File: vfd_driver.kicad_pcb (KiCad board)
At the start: 2 copper layers, 89.5 x 45.3 mm, 34 parts, among them J1 Input, J2 futaba_7_lt_44z, J3 High Volt, J4 FIL_n, J5 FIL_p, Q3 BC817, Q4 BC807, Q5 BC817, Q6 BC807, U1 74HC595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

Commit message: before adding lt1073
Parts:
- removed C1: 10u, Capacitor_THT:CP_Radial_D8.0mm_P3.80mm
- removed C2: 100n, Capacitor_SMD:C_0805_2012Metric_Pad1.15x1.40mm_HandSolder
- removed J4: FIL_n, Connector_Pin:Pin_D1.4mm_L8.5mm_W2.8mm_FlatFork
- removed J5: FIL_p, Connector_Pin:Pin_D1.4mm_L8.5mm_W2.8mm_FlatFork
- removed L2: 33, Inductor_SMD:L_1206_3216Metric_Pad1.42x1.75mm_HandSolder
- removed Q3, Q5: BC817, Package_TO_SOT_SMD:SOT-23
- removed Q4, Q6: BC807, Package_TO_SOT_SMD:SOT-23
- removed R10, R7, R8: 33k, Resistor_SMD:R_0805_2012Metric_Pad1.15x1.40mm_HandSolder
- removed R12, R13: 0, Resistor_SMD:R_1206_3216Metric
- removed R6, R9: 100k, Resistor_SMD:R_0805_2012Metric_Pad1.15x1.40mm_HandSolder
- removed U2, U3, U4: 74HC595, Package_SO:SOIC-16_3.9x9.9mm_P1.27mm
- removed U5, U6, U7: TBD62783A, Package_SO:SOP-18_7.0x12.5mm_P1.27mm
- added C4: 10u/63v, Capacitor_THT:CP_Radial_D8.0mm_P5.00mm, F.Cu at (41.9, 56.6)
- added C6: 4n7, Capacitor_SMD:C_0805_2012Metric_Pad1.15x1.40mm_HandSolder, B.Cu at (63.1, 46.6)
- added C7: 1u, Capacitor_THT:C_Rect_L7.0mm_W2.0mm_P5.00mm, F.Cu at (57.9, 44.2)
- added C8: 100n, Capacitor_THT:C_Rect_L7.0mm_W2.0mm_P5.00mm, F.Cu at (53.0, 41.4)
- added C9: 10n, Capacitor_SMD:C_0805_2012Metric_Pad1.15x1.40mm_HandSolder, B.Cu at (45.1, 43.0)
- added D2: SS14, Diode_SMD:D_SMA_Handsoldering, B.Cu at (51.1, 50.7)
- added D3: 1N4148, Diode_SMD:D_MiniMELF, B.Cu at (55.6, 37.9)
- added L1: 330, Choke_SMD:Choke_CD75, B.Cu at (42.8, 50.0)
- added Q1: IRLZ34, Package_TO_SOT_THT:TO-220-3_Vertical, F.Cu at (33.5, 51.2)
- added R14: 0, Resistor_SMD:R_1206_3216Metric, B.Cu at (44.5, 36.4)
- added R15: 22k, Resistor_SMD:R_0805_2012Metric_Pad1.15x1.40mm_HandSolder, B.Cu at (63.1, 43.9)
- added R16: 18, Resistor_SMD:R_1206_3216Metric_Pad1.42x1.75mm_HandSolder, B.Cu at (64.8, 53.2)
- added R17: 18, Resistor_SMD:R_1206_3216Metric_Pad1.42x1.75mm_HandSolder, B.Cu at (55.8, 59.3)
- added R18: 4k7, Resistor_SMD:R_0805_2012Metric_Pad1.15x1.40mm_HandSolder, B.Cu at (52.6, 37.5)
- added R3: 22k, Resistor_SMD:R_0805_2012Metric_Pad1.15x1.40mm_HandSolder, B.Cu at (64.1, 41.4)
- added R4: 10k, Resistor_SMD:R_0805_2012Metric_Pad1.15x1.40mm_HandSolder, B.Cu at (58.2, 47.4)
- added U8: LM555, Package_DIP:DIP-8_W7.62mm_Socket_LongPads, F.Cu at (40.8, 33.5)
- C5: value 10n -> 100n
- D1: value SD103BW -> SD_103BW
- J1: footprint Connector_PinSocket_2.54mm:PinSocket_1x07_P2.54mm_Vertical -> Connector_PinHeader_2.54mm:PinHeader_1x02_P2.54mm_Vertical
- J2: value futaba_7_lt_44z -> FIL; footprint Connector_PinSocket_2.54mm:PinSocket_1x34_P2.54mm_Vertical -> Connector_PinHeader_2.54mm:PinHeader_1x02_P2.54mm_Vertical; moved to F.Cu
- J3: value High Volt -> HV
- R1: value 0 -> 1k; footprint Resistor_SMD:R_1206_3216Metric -> Resistor_SMD:R_0805_2012Metric_Pad1.15x1.40mm_HandSolder
- R2: value 0 -> 100k; footprint Resistor_SMD:R_1206_3216Metric -> Resistor_SMD:R_0805_2012Metric_Pad1.15x1.40mm_HandSolder
- R5: value 33k -> 1k
- U1: value 74HC595 -> LM4871; footprint Package_SO:SOIC-16_3.9x9.9mm_P1.27mm -> Package_SO:SOIC-8_3.9x4.9mm_P1.27mm
- moved H2 91.6 mm to (31.6, 58.4)
- moved R2 73.2 mm to (35.3, 41.0)
- moved C5 64.5 mm to (44.7, 31.8), turned to 180 degrees
- moved R5 62.7 mm to (58.5, 37.6), turned to 270 degrees
- moved U1 53.8 mm to (58.2, 53.0), turned to 270 degrees
- moved R1 53.5 mm to (35.3, 38.0)
- moved C3 43.8 mm to (63.8, 34.7), turned to 270 degrees
- moved D1 37.3 mm to (36.7, 47.4), turned to 90 degrees
- moved J2 28.3 mm to (62.5, 59.3)
- moved J3 14.1 mm to (50.0, 59.3), turned to 270 degrees
- moved J1 9.29 mm to (54.7, 32.9), turned to 90 degrees
- moved H1 5.66 mm to (31.6, 33.4)
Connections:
- C3 pad 1: VCC -> +5V
- C5 pad 1: VCC -> +5V
- D1 pad 2: VDD -> GND
- J1 pad 2: VDD -> +5V
- J2 pad 1: Net-(J2-Pad1) -> /FIL_n
- J2 pad 2: (no net) -> /FIL_p
- J3 pad 1: GND -> +36V
- J3 pad 2: +36V -> GND
- R1 pad 1: /SRCLK -> Net-(Q1-Pad1)
- R1 pad 2: /SRCLK -> /HV
- R2 pad 1: /SRCLK -> Net-(Q1-Pad1)
- R2 pad 2: /SRCLK -> GND
- R5 pad 1: /Q4G -> +5V
- U1 pad 1: (no net) -> GND
- U1 pad 2: (no net) -> Net-(C7-Pad1)
- U1 pad 3: (no net) -> Net-(R15-Pad2)
- U1 pad 4: (no net) -> Net-(C6-Pad1)
- U1 pad 5: (no net) -> Net-(R15-Pad1)
- U1 pad 6: /Q4G -> +5V
- U1 pad 7: /Q4H -> GND
- U1 pad 8: GND -> Net-(R17-Pad1)
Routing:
- net VCC: track 119.9 -> 0.00 mm, vias 4 -> 0
- net /~SRCLR: track 109.7 -> 0.00 mm, vias 2 -> 0
- net /RCLK: track 94.4 -> 0.00 mm, vias 6 -> 0
- net /SRCLK: track 93.5 -> 0.00 mm, vias 2 -> 0
- net +5V: track 0.00 -> 81.7 mm
- net +36V: track 95.8 -> 18.2 mm
- net /Q1: track 48.7 -> 0.00 mm, vias 2 -> 0
- net /Q0: track 45.6 -> 0.00 mm, vias 2 -> 0
- net /Q2: track 35.3 -> 0.00 mm, vias 2 -> 0
- net Net-(R15-Pad1): track 0.00 -> 27.1 mm
- net /G1: track 21.3 -> 0.00 mm
- net Net-(C8-Pad1): track 0.00 -> 21.2 mm
- net /S10: track 21.1 -> 0.00 mm
- net /G5: track 19.9 -> 0.00 mm
- net Net-(Q1-Pad1): track 0.00 -> 17.9 mm
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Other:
- board size 89.5 x 45.3 mm -> 41.3 x 32.6 mm
- board text removed: "VFD-DRIVER"

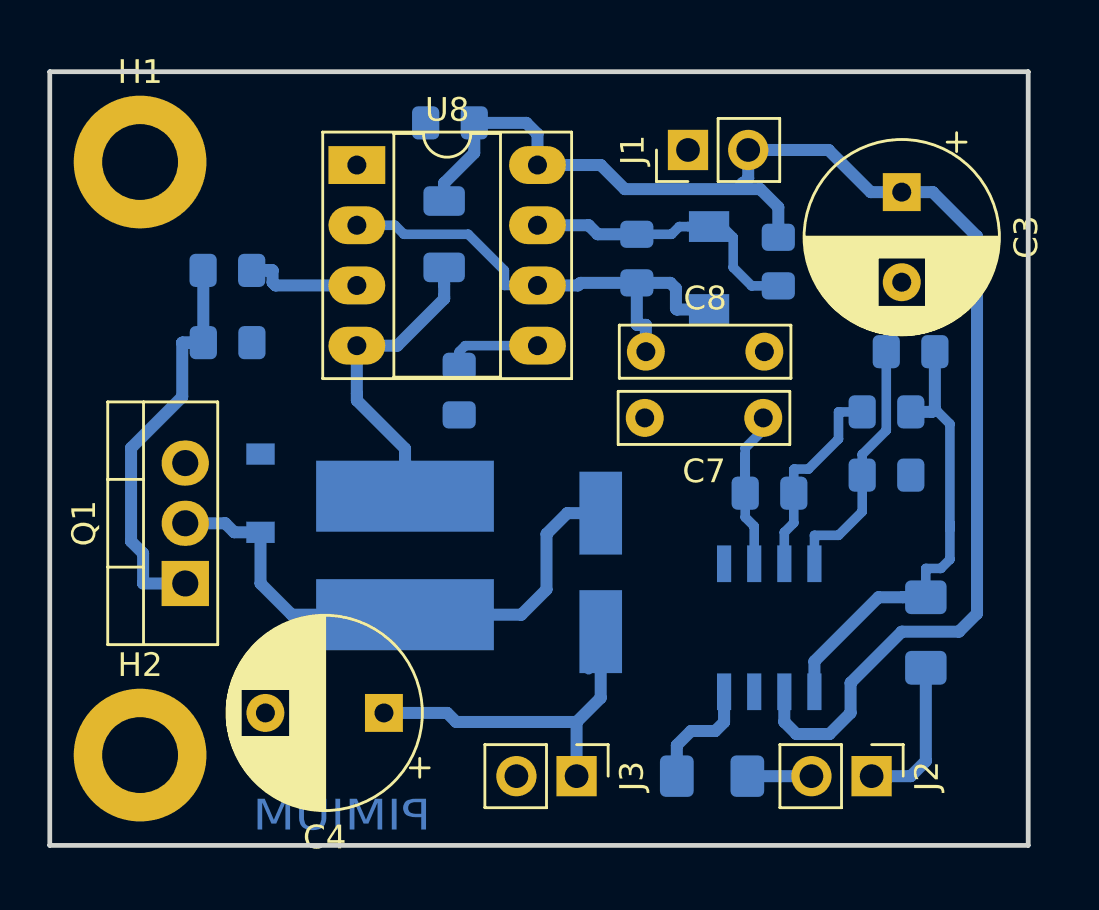
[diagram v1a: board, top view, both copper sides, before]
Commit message: Separated input for the step up driver so ca be supply with 12V.
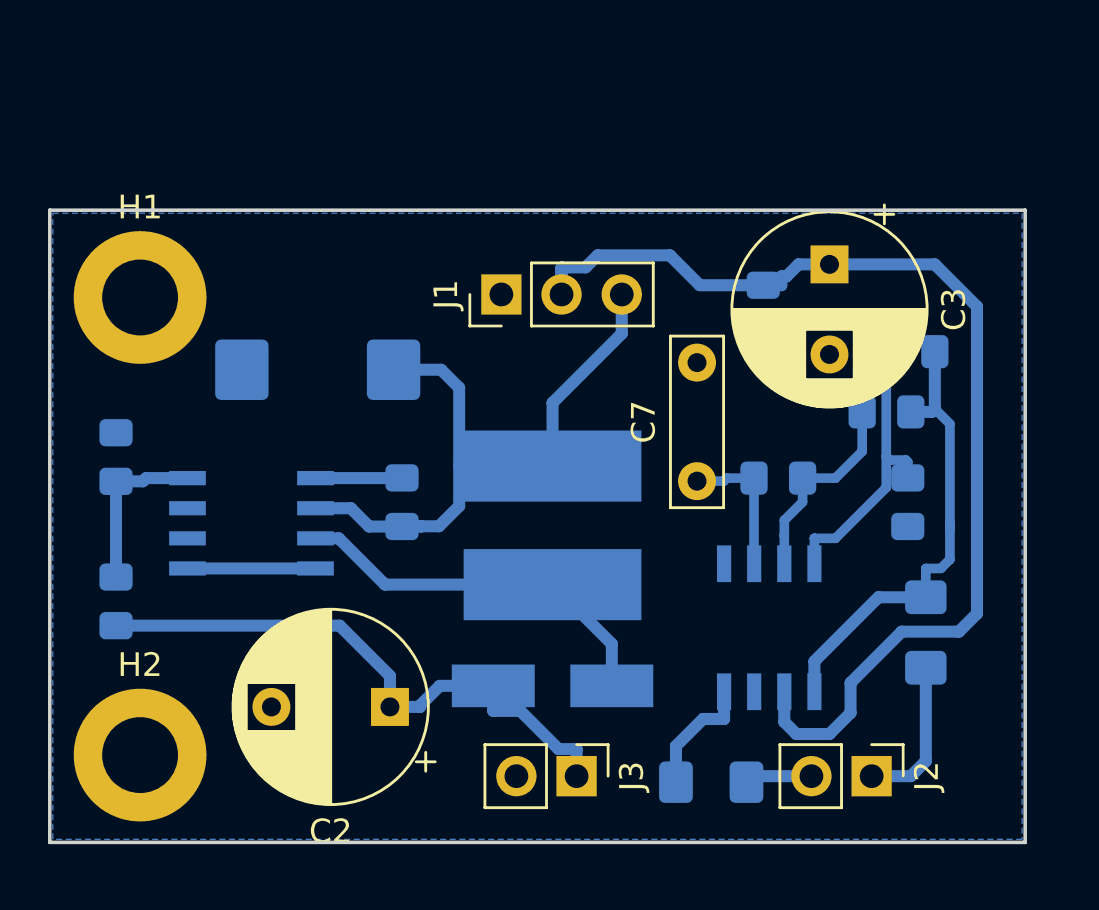
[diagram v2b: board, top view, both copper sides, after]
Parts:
- removed C4: 10u/63v, Capacitor_THT:CP_Radial_D8.0mm_P5.00mm
- removed C8: 100n, Capacitor_THT:C_Rect_L7.0mm_W2.0mm_P5.00mm
- removed C9: 10n, Capacitor_SMD:C_0805_2012Metric_Pad1.15x1.40mm_HandSolder
- removed D2: SS14, Diode_SMD:D_SMA_Handsoldering
- removed D3: 1N4148, Diode_SMD:D_MiniMELF
- removed Q1: IRLZ34, Package_TO_SOT_THT:TO-220-3_Vertical
- removed R14: 0, Resistor_SMD:R_1206_3216Metric
- removed R18: 4k7, Resistor_SMD:R_0805_2012Metric_Pad1.15x1.40mm_HandSolder
- removed U8: LM555, Package_DIP:DIP-8_W7.62mm_Socket_LongPads
- added C1: 100u, Capacitor_Tantalum_SMD:CP_EIA-7343-15_Kemet-W_Pad2.25x2.55mm_HandSolder, B.Cu at (39.1, 42.2)
- added C2: 100u/63v, Capacitor_THT:CP_Radial_D8.0mm_P5.00mm, F.Cu at (42.2, 56.4)
- added U2: LT1073CS, Package_SO:SOIC-8_3.9x4.9mm_P1.27mm, B.Cu at (36.3, 48.6)
- D1: value SD_103BW -> SS14; footprint Diode_SMD:D_SOD-123 -> Diode_SMD:D_SMA_Handsoldering
- J1: value Input -> INPUT; footprint Connector_PinHeader_2.54mm:PinHeader_1x02_P2.54mm_Vertical -> Connector_PinHeader_2.54mm:PinHeader_1x03_P2.54mm_Vertical
- R1: value 1k -> 50
- R2: value 100k -> 1M
- R5: value 1k -> 10k
- moved R5 29.1 mm to (30.6, 45.8)
- moved C5 15.4 mm to (57.9, 39.6), turned to 270 degrees
- moved D1 14.8 mm to (49.0, 55.5), turned to 0 degrees
- moved R1 12.2 mm to (42.7, 47.8), turned to 270 degrees
- moved R2 11.9 mm to (30.6, 51.9), turned to 270 degrees
- moved J1 9.96 mm to (46.9, 39.0)
- moved L1 6.35 mm to (49.0, 48.7)
- moved H1 5.71 mm to (31.6, 39.1)
- moved C3 4.31 mm to (60.7, 37.7)
- moved C7 3.86 mm to (55.1, 46.9), turned to 90 degrees
- moved C6 1.45 mm to (64.0, 47.8), turned to 270 degrees
- moved R4 0.74 mm to (58.5, 46.7)
- moved R17 0.26 mm to (55.7, 59.6)
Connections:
- D1 pad 1: Net-(D1-Pad1) -> +36V
- D1 pad 2: GND -> Net-(D1-Pad2)
- L1 pad 1: +5V -> +12V
- L1 pad 2: Net-(D1-Pad1) -> Net-(D1-Pad2)
- R1 pad 1: Net-(Q1-Pad1) -> Net-(R1-Pad1)
- R1 pad 2: /HV -> +12V
- R2 pad 1: Net-(Q1-Pad1) -> Net-(R2-Pad1)
- R2 pad 2: GND -> +36V
- R5 pad 1: +5V -> GND
- R5 pad 2: Net-(D3-Pad2) -> Net-(R2-Pad1)
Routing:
- net +5V: track 81.7 -> 46.8 mm
- net +12V: track 0.00 -> 27.2 mm
- net Net-(D1-Pad1): track 23.5 -> 0.00 mm
- net Net-(C8-Pad1): track 21.2 -> 0.00 mm
- net Net-(Q1-Pad1): track 17.9 -> 0.00 mm
- net Net-(D1-Pad2): track 0.00 -> 16.1 mm
- net Net-(D3-Pad2): track 13.5 -> 0.00 mm
- net Net-(R2-Pad1): track 0.00 -> 7.11 mm
- net +36V: track 18.2 -> 25.0 mm
- net /HV: track 5.41 -> 0.00 mm
- net GND: track 0.00 -> 5.40 mm
- net Net-(C9-Pad1): track 4.02 -> 0.00 mm
- net Net-(R1-Pad1): track 0.00 -> 3.65 mm
- net Net-(C7-Pad1): track 9.16 -> 6.07 mm
- net Net-(C6-Pad1): track 10.9 -> 12.4 mm
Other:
- board size 41.3 x 32.6 mm -> 41.1 x 26.7 mm

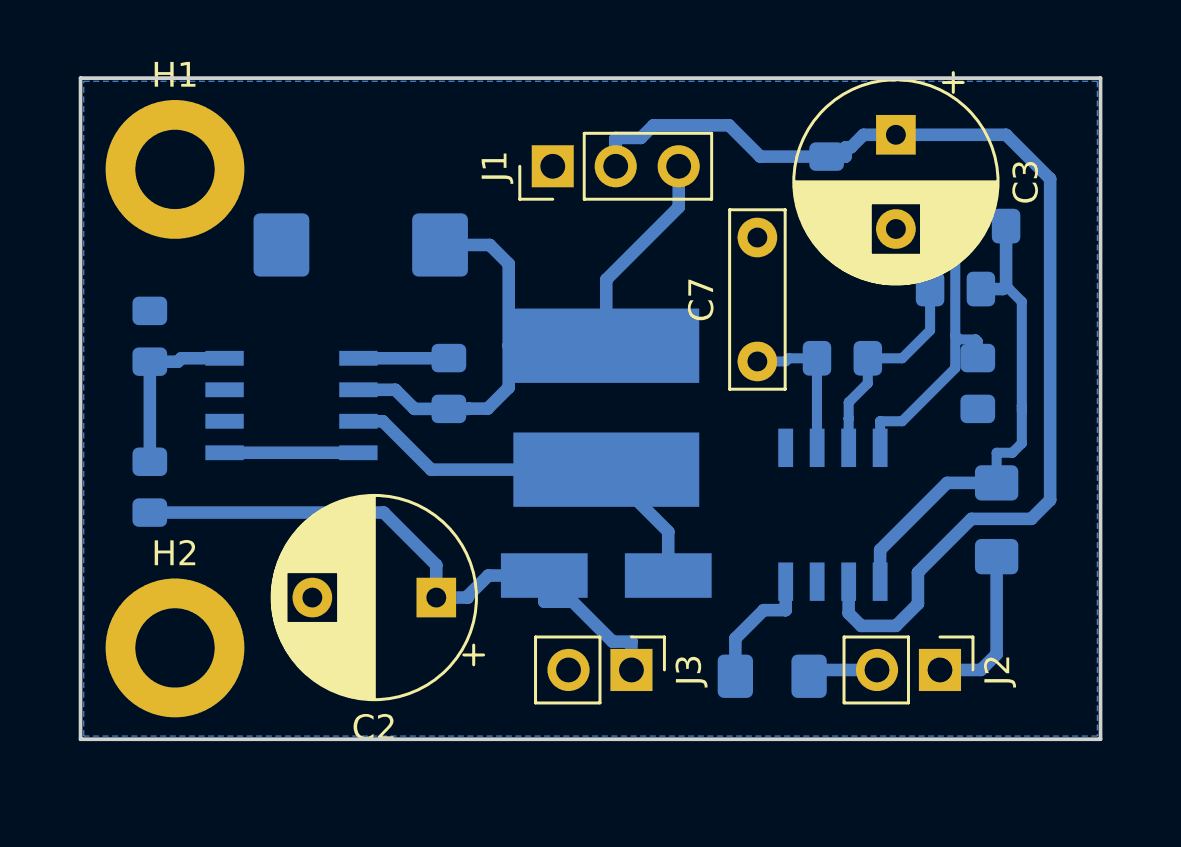
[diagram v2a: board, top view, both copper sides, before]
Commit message: add marks that helps, when the board is drilled.
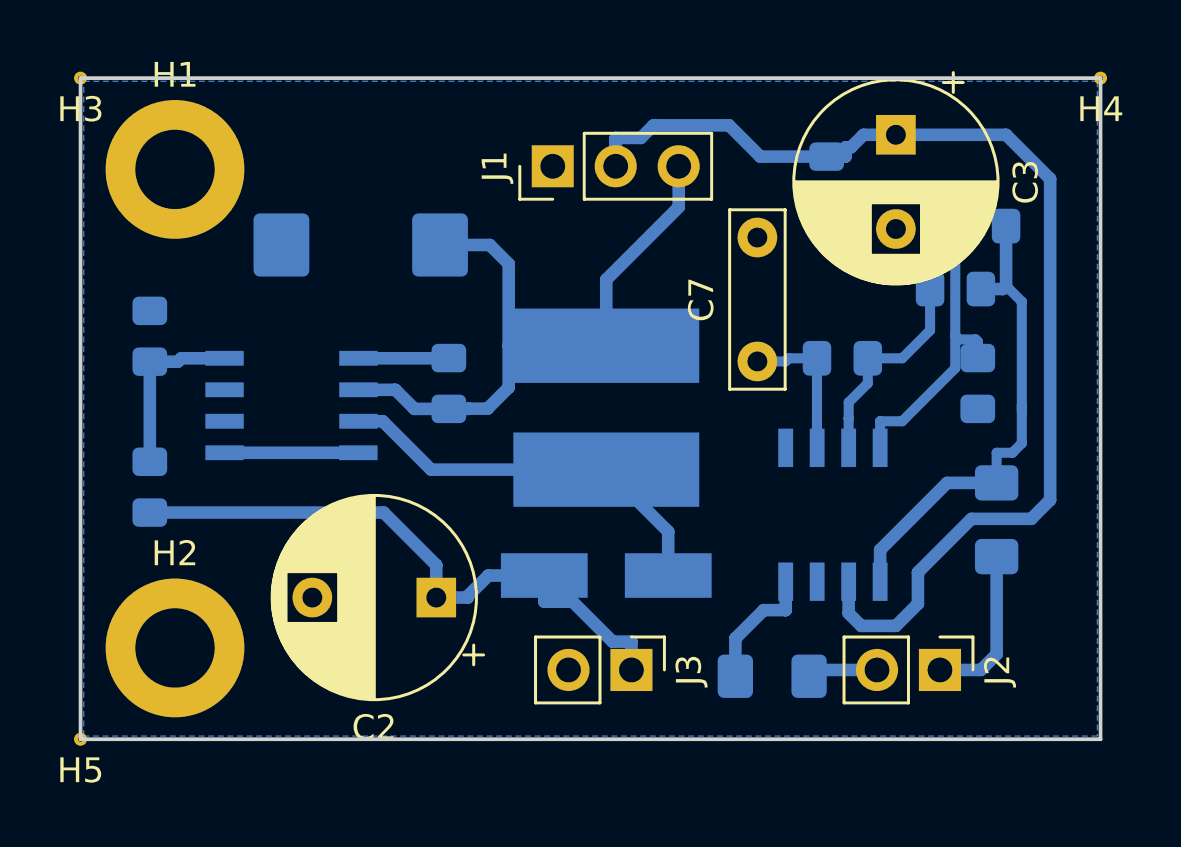
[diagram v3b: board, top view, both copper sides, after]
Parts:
- added H3: MH, custom_footprint:markierung, F.Cu at (27.8, 35.4)
- added H4: MH, custom_footprint:markierung, F.Cu at (69.0, 35.4)
- added H5: MH, custom_footprint:markierung, F.Cu at (27.8, 62.1)
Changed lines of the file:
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@@
     (tracks 115)
     (zones 0)
-    (modules 23)
+    (modules 26)
     (nets 15)
   )
@@
   )
   (setup
-    (last_trace_width 0.508)
+    (last_trace_width 0.25)
     (user_trace_width 0.4064)
     (user_trace_width 0.508)
@@
     )
   )
+  (module custom_footprint:markierung (layer F.Cu)
+    (at 27.813 35.433)
+    (fp_text reference H3 (at 0 1.27) (layer F.SilkS)
+      (effects (font (size 1 1) (thickness 0.15)))
+    )
+    (fp_text value MH (at 0 -1.27) (layer F.Fab)
+      (effects (font (size 1 1) (thickness 0.15)))
+    )
+    (pad 1 thru_hole circle (at 0 0) (size 0.524 0.524) (drill 0.2) (layers *.Cu *.Mask))
+  )
+  (module custom_footprint:markierung (layer F.Cu)
+    (at 68.961 35.433)
+    (fp_text reference H4 (at 0 1.27) (layer F.SilkS)
+      (effects (font (size 1 1) (thickness 0.15)))
+    )
+    (fp_text value MH (at 0 -1.27) (layer F.Fab)
+      (effects (font (size 1 1) (thickness 0.15)))
+    )
+    (pad 1 thru_hole circle (at 0 0) (size 0.524 0.524) (drill 0.2) (layers *.Cu *.Mask))
+  )
+  (module custom_footprint:markierung (layer F.Cu)
+    (at 27.813 62.103)
+    (fp_text reference H5 (at 0 1.27) (layer F.SilkS)
+      (effects (font (size 1 1) (thickness 0.15)))
+    )
+    (fp_text value MH (at 0 -1.27) (layer F.Fab)
+      (effects (font (size 1 1) (thickness 0.15)))
+    )
+    (pad 1 thru_hole circle (at 0 0) (size 0.524 0.524) (drill 0.2) (layers *.Cu *.Mask))
+  )
   (gr_line (start 27.813 62.103) (end 27.813 35.433) (layer Edge.Cuts) (width 0.15))
   (gr_line (start 68.961 62.103) (end 27.813 62.103) (layer Edge.Cuts) (width 0.15))
@@
   (segment (start 60.706 37.719) (end 65.151 37.719) (width 0.508) (layer B.Cu) (net 3) (status 10))
   (segment (start 66.929 39.497) (end 66.929 52.451) (width 0.508) (layer B.Cu) (net 3))
-  (segment (start 39.022 48.006) (end 40.513 48.006) (width 0.508) (layer B.Cu) (net 14) (status 10))
-  (segment (start 41.284 48.777) (end 42.672 48.777) (width 0.508) (layer B.Cu) (net 14) (status 20))
-  (segment (start 40.513 48.006) (end 41.284 48.777) (width 0.508) (layer B.Cu) (net 14))
-  (segment (start 42.672 48.777) (end 43.472 48.777) (width 0.508) (layer B.Cu) (net 14) (status 10))
-  (segment (start 43.481 48.768) (end 44.232 48.768) (width 0.508) (layer B.Cu) (net 14))
-  (segment (start 43.472 48.777) (end 43.481 48.768) (width 0.508) (layer B.Cu) (net 14))
-  (segment (start 45.085 47.915) (end 44.232 48.768) (width 0.508) (layer B.Cu) (net 14))
-  (segment (start 45.085 46.228) (end 45.085 47.915) (width 0.508) (layer B.Cu) (net 14))
-  (segment (start 49.022 46.228) (end 45.085 46.228) (width 0.508) (layer B.Cu) (net 14) (status 10))
   (segment (start 49.403 38.481) (end 49.403 37.846) (width 0.508) (layer B.Cu) (net 3))
   (segment (start 59.398 37.719) (end 60.706 37.719) (width 0.508) (layer B.Cu) (net 3))
@@
   (segment (start 50.927 37.338) (end 53.975 37.338) (width 0.508) (layer B.Cu) (net 3))
   (segment (start 53.975 37.338) (end 55.236 38.599) (width 0.508) (layer B.Cu) (net 3))
-  (segment (start 42.316 42.164) (end 44.323 42.164) (width 0.508) (layer B.Cu) (net 14))
-  (segment (start 45.085 42.926) (end 45.085 46.228) (width 0.508) (layer B.Cu) (net 14))
-  (segment (start 44.323 42.164) (end 45.085 42.926) (width 0.508) (layer B.Cu) (net 14))
   (segment (start 64.135 59.309) (end 62.484 59.309) (width 0.508) (layer B.Cu) (net 4) (status 20))
   (segment (start 64.77 58.674) (end 64.135 59.309) (width 0.508) (layer B.Cu) (net 4))
@@
   (segment (start 31.877 46.736) (end 33.622 46.736) (width 0.508) (layer B.Cu) (net 13) (status 20))
   (segment (start 31.741 46.872) (end 31.877 46.736) (width 0.508) (layer B.Cu) (net 13))
+  (segment (start 39.022 48.006) (end 40.513 48.006) (width 0.508) (layer B.Cu) (net 14) (status 10))
+  (segment (start 41.284 48.777) (end 42.672 48.777) (width 0.508) (layer B.Cu) (net 14) (status 20))
+  (segment (start 40.513 48.006) (end 41.284 48.777) (width 0.508) (layer B.Cu) (net 14))
+  (segment (start 42.672 48.777) (end 43.472 48.777) (width 0.508) (layer B.Cu) (net 14) (status 10))
+  (segment (start 43.481 48.768) (end 44.232 48.768) (width 0.508) (layer B.Cu) (net 14))
+  (segment (start 43.472 48.777) (end 43.481 48.768) (width 0.508) (layer B.Cu) (net 14))
+  (segment (start 45.085 47.915) (end 44.232 48.768) (width 0.508) (layer B.Cu) (net 14))
+  (segment (start 45.085 46.228) (end 45.085 47.915) (width 0.508) (layer B.Cu) (net 14))
+  (segment (start 49.022 46.228) (end 45.085 46.228) (width 0.508) (layer B.Cu) (net 14) (status 10))
+  (segment (start 42.316 42.164) (end 44.323 42.164) (width 0.508) (layer B.Cu) (net 14))
+  (segment (start 45.085 42.926) (end 45.085 46.228) (width 0.508) (layer B.Cu) (net 14))
+  (segment (start 44.323 42.164) (end 45.085 42.926) (width 0.508) (layer B.Cu) (net 14))
   (segment (start 49.022 43.561) (end 49.022 46.228) (width 0.508) (layer B.Cu) (net 14))
   (segment (start 51.943 40.64) (end 49.022 43.561) (width 0.508) (layer B.Cu) (net 14))
